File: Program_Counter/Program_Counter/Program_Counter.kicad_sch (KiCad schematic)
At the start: 3 parts

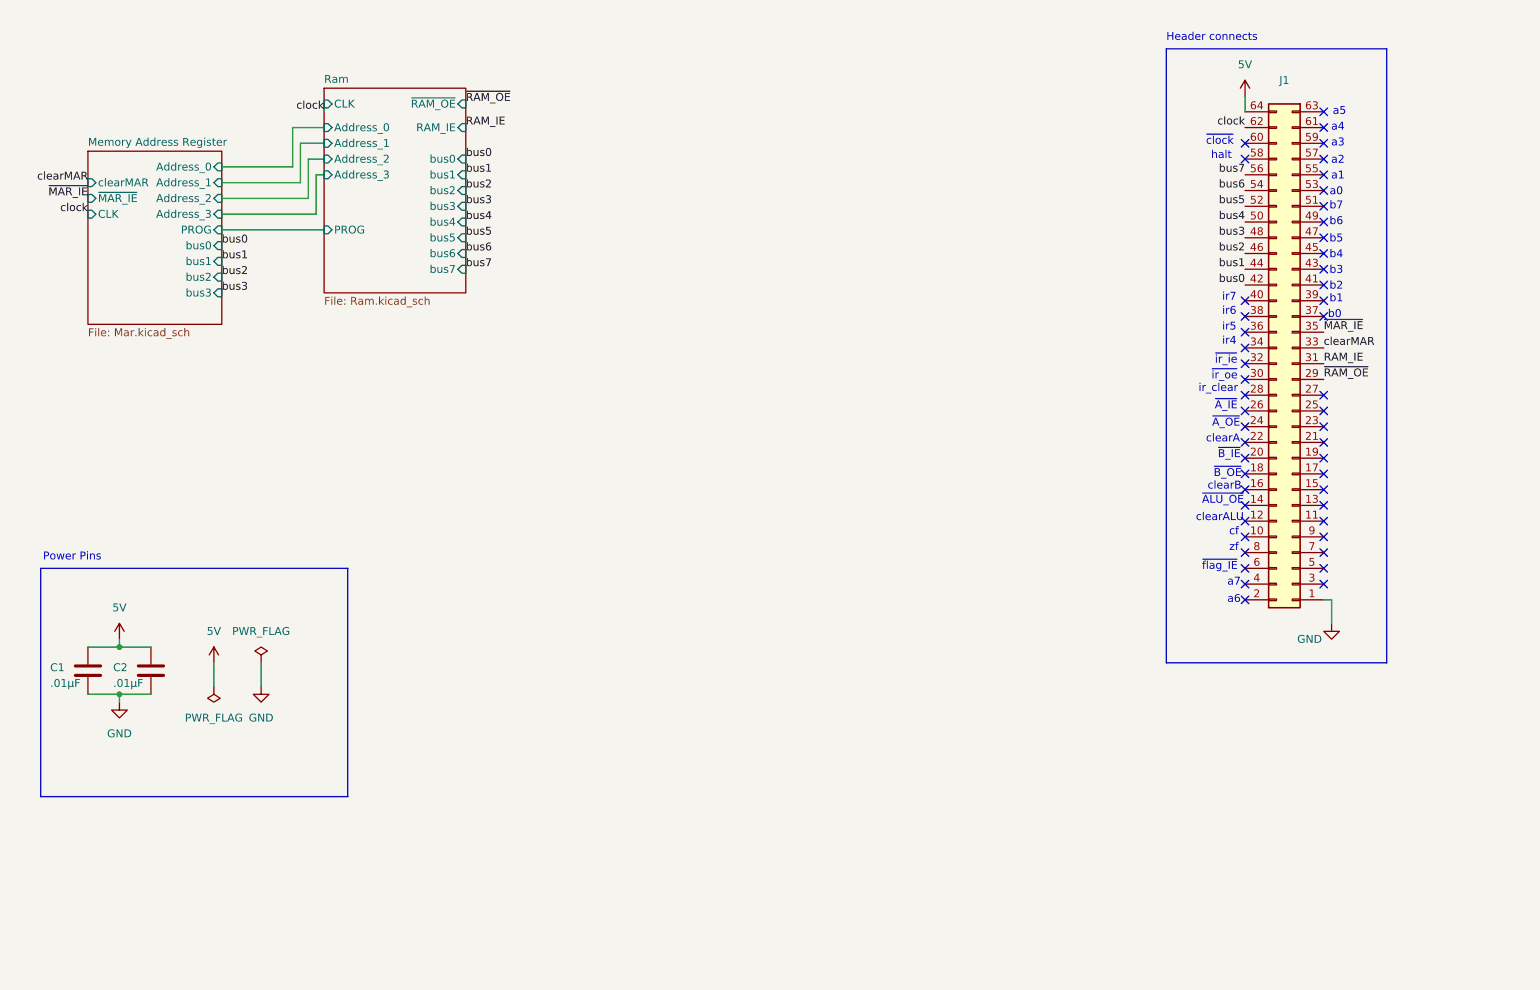
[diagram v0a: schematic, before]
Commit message: Added Program Counter Schematic
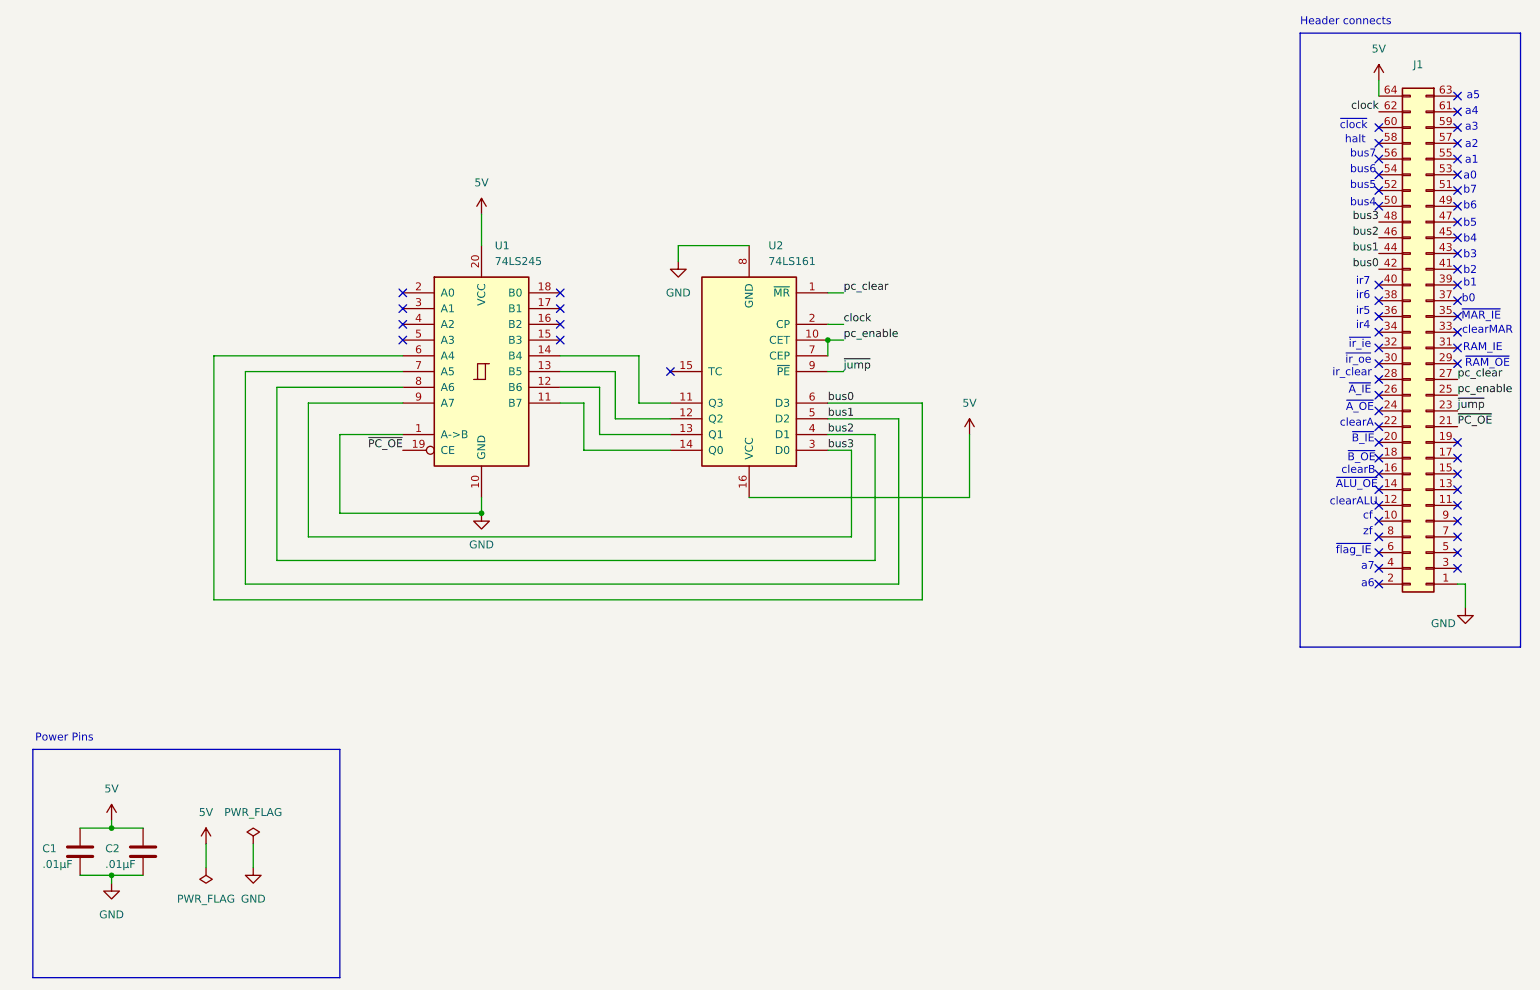
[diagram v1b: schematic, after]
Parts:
- added U1: 74LS245, symbol 74xx:74LS245
- added U2: 74LS161, symbol 74xx:74LS161
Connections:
- net 5V: now also U1.20 (VCC), U2.16 (VCC)
- net GND: now also U1.1 (A->B), U1.10 (GND), U2.8 (GND)
- net bus0: now also U1.6 (A4), U2.6 (D3)
- net bus1: now also U1.7 (A5), U2.5 (D2)
- net bus2: now also U1.8 (A6), U2.4 (D1)
- net bus3: now also U1.9 (A7), U2.3 (D0)
- net clock: now also U2.2 (CP)
- net ~{PC_OE}: now reaches J1.21
- net ~{PC_OE}: now also U1.19 (CE)
- net ~{jump}: now reaches J1.23
- net ~{jump}: now also U2.9 (~{PE})
- net pc_enable: now reaches J1.25
- net pc_enable: now also U2.10 (CET), U2.7 (CEP)
- net pc_clear: now reaches J1.27
- net pc_clear: now also U2.1 (~{MR})
- net RAM_IE: no longer names the net of J1.31
- net bus4: no longer names the net of J1.50
- net bus5: no longer names the net of J1.52
- net bus6: no longer names the net of J1.54
- net bus7: no longer names the net of J1.56
- net clearMAR: no longer names the net of J1.33
- net ~{MAR_IE}: no longer names the net of J1.35
- net ~{RAM_OE}: no longer names the net of J1.29
- new net: U1.14 (B4), U2.11 (Q3)
- new net: U1.13 (B5), U2.12 (Q2)
- new net: U1.12 (B6), U2.13 (Q1)
- new net: U1.11 (B7), U2.14 (Q0)
- no-connect marks 49 -> 62
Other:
- removed sheet Memory Address Register
- removed sheet Ram
- note added: "RAM_IE"
- note added: "bus4"
- note added: "bus5"
- note added: "bus6"
- note added: "bus7"
- note added: "clearMAR"
- note added: "~{MAR_IE}"
- note added: "~{RAM_OE}"
- company: Arsenal Gear -> (none)
- title: Ram Module -> (none)
- moved on the sheet: C1, C2, J1
